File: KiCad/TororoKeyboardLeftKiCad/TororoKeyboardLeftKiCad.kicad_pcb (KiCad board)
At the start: 2 copper layers, 139.7 x 99.2 mm, 97 parts, among them J1 MJ-4PP-9, SW1 SW_PUSH, SW10 SW_PUSH, SW11 SW_PUSH, SW12 SW_PUSH, SW13 SW_PUSH, SW14 SW_PUSH, SW15 SW_PUSH, SW16 SW_PUSH, SW17 SW_PUSH, SW18 SW_PUSH, SW19 SW_PUSH, SW2 SW_PUSH, SW20 SW_PUSH, SW21 SW_PUSH, SW22 SW_PUSH, SW23 SW_PUSH, SW24 SW_PUSH, SW25 SW_PUSH, SW26 SW_PUSH, SW27 SW_PUSH, SW28 SW_PUSH, SW29 SW_PUSH, SW3 SW_PUSH, SW4 SW_PUSH, SW5 SW_PUSH, SW6 SW_PUSH, SW7 SW_PUSH, SW8 SW_PUSH, SW9 SW_PUSH, U1 ProMicro

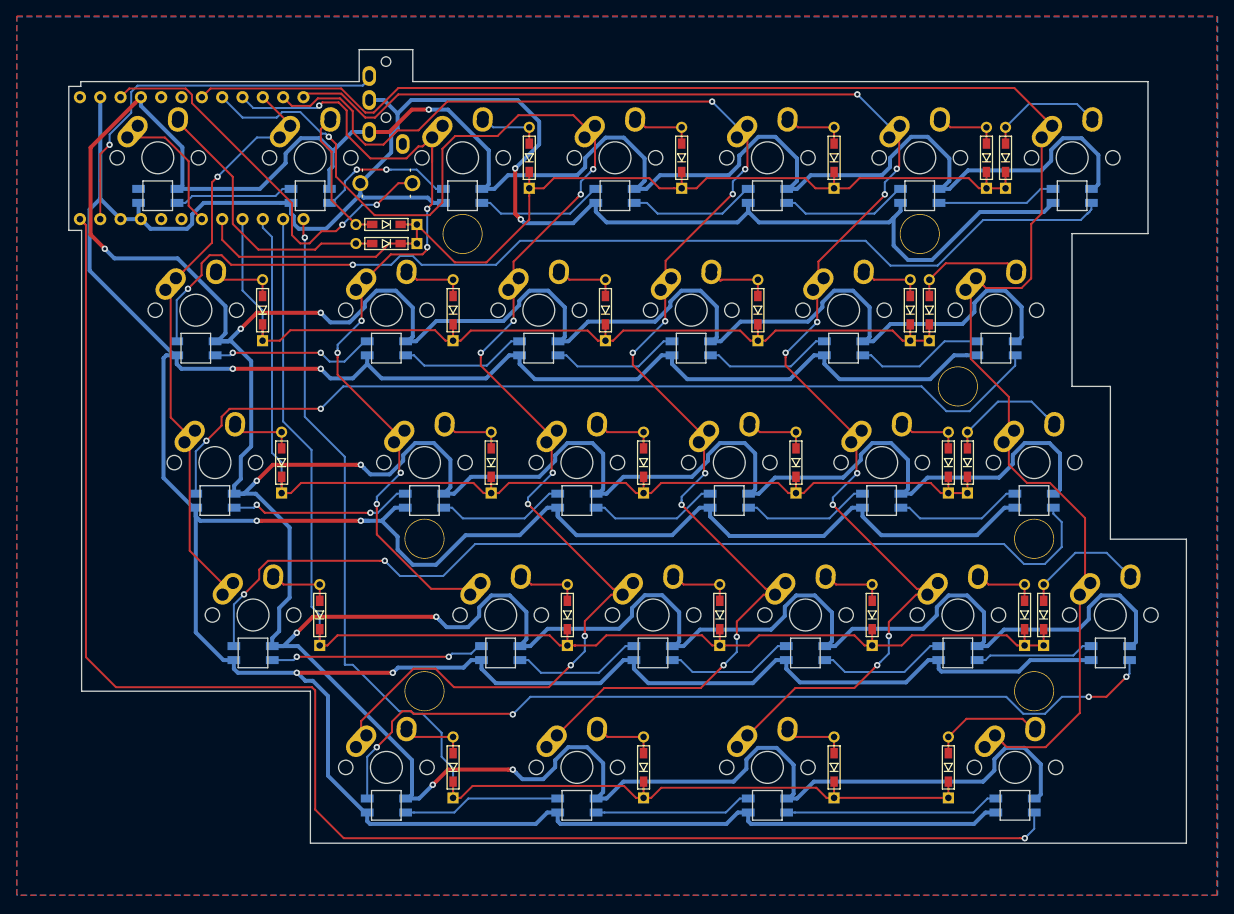
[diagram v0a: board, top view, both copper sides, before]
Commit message: 左手側の配線を修正
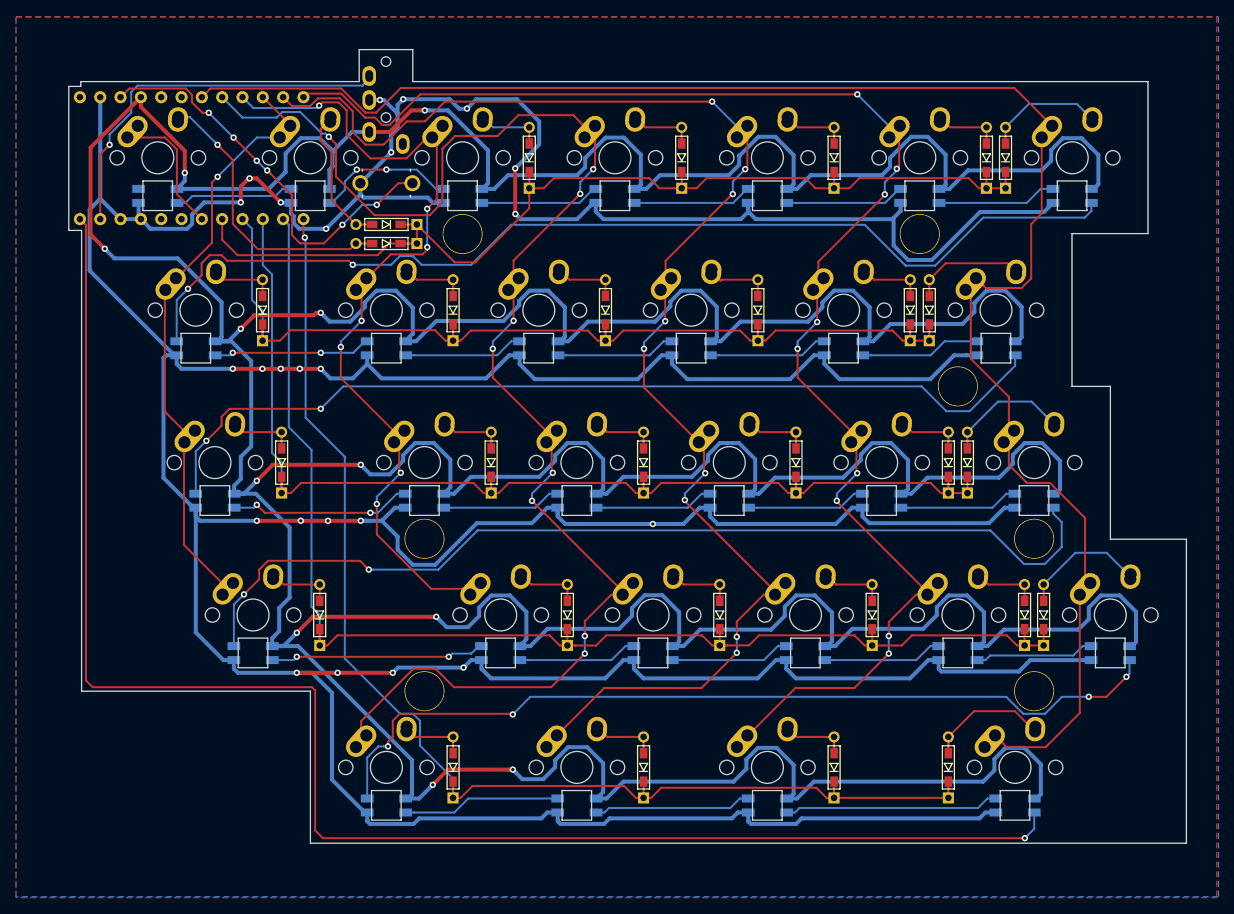
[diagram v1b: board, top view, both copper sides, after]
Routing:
- net led: track 195.0 -> 198.2 mm
- net col3: track 110.9 -> 108.1 mm
- net VCC: track 877.7 -> 875.2 mm, vias 10 -> 11
- net col4: track 186.0 -> 183.9 mm
- net col5: track 178.9 -> 176.9 mm
- net Net-(L25-Pad3): track 130.4 -> 132.1 mm
- net col6: track 185.7 -> 184.2 mm
- net Net-(D1-Pad2): track 34.7 -> 36.1 mm, vias 0 -> 1
- net Net-(L13-Pad1): track 16.3 -> 15.0 mm
- net col2: track 71.7 -> 72.9 mm
- net Net-(L13-Pad3): track 16.2 -> 15.0 mm
- net Net-(L18-Pad3): track 16.2 -> 15.0 mm
- net row5: track 154.5 -> 153.4 mm
- net Net-(L21-Pad3): track 16.1 -> 15.0 mm
- net Net-(L16-Pad3): track 16.1 -> 15.0 mm
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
